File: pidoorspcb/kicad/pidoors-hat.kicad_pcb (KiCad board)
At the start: 2 copper layers, 65 x 56.5 mm, 4 parts

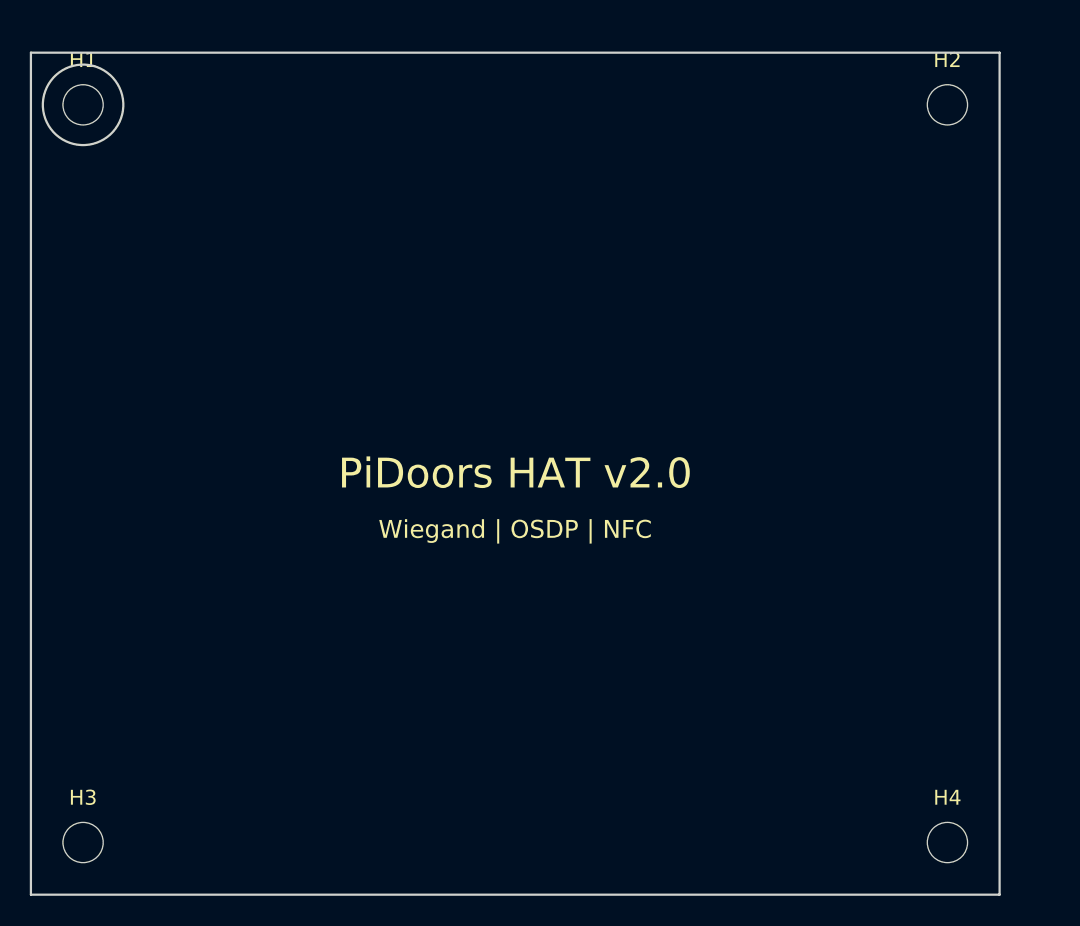
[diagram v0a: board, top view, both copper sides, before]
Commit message: PCB: Complete routing and generate Gerber manufacturing files
- Fix GPIO discrepancy: LED Granted now uses GPIO 25 (was GPIO 5)
- Fix README: Relay uses GPIO 18 (was incorrectly listed as GPIO 17)
- Complete KiCad schematic with all component symbols and connections
- Route PCB with power traces (0.5mm) and signal traces (0.25mm)
- Add ground plane on bottom copper layer
- Generate Gerber files in RS-274X format for JLCPCB
- Generate Excellon drill files (PTH and NPTH)
- Add manufacturing checklist with ordering instructions
- Add gerber generation script for KiCad 8.x

Co-Authored-By: Claude Opus 4.5 <noreply@anthropic.com>
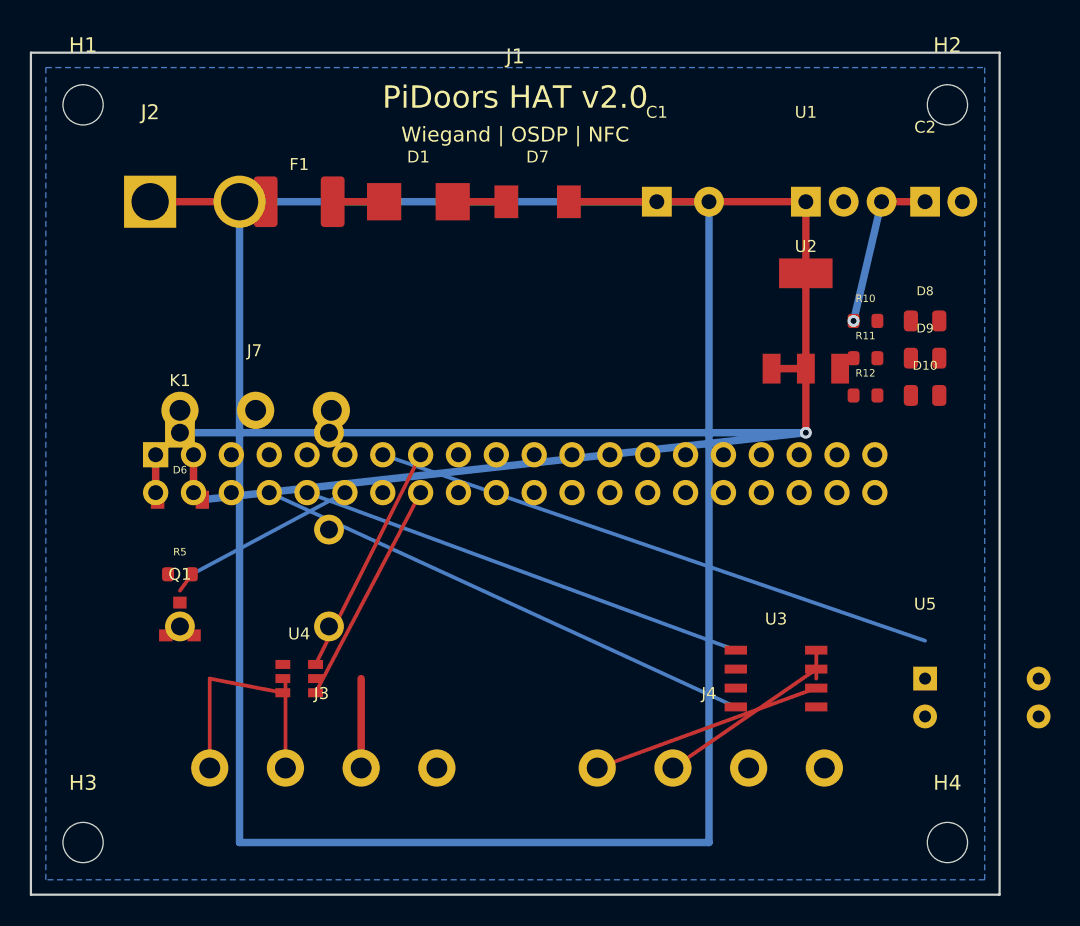
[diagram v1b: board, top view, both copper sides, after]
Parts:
- added C1: 100uF/35V, Capacitor_THT:CP_Radial_D8.0mm_P3.50mm, F.Cu at (42.0, 10.0)
- added C2: 100uF/10V, Capacitor_THT:CP_Radial_D6.3mm_P2.50mm, F.Cu at (60.0, 10.0)
- added D1: SMBJ24A, Diode_SMD:D_SMB, F.Cu at (26.0, 10.0)
- added D10: ERR, LED_SMD:LED_0805_2012Metric, F.Cu at (60.0, 23.0)
- added D6: 1N4148W, Diode_SMD:D_SOD-123, F.Cu at (10.0, 30.0)
- added D7: SS34, Diode_SMD:D_SMA, F.Cu at (34.0, 10.0)
- added D8: PWR, LED_SMD:LED_0805_2012Metric, F.Cu at (60.0, 18.0)
- added D9: OK, LED_SMD:LED_0805_2012Metric, F.Cu at (60.0, 20.5)
- added F1: 1.1A, Fuse:Fuse_1812_4532Metric, F.Cu at (18.0, 10.0)
- added J1: Raspberry_Pi, Connector_PinSocket_2.54mm:PinSocket_2x20_P2.54mm_Vertical, F.Cu at (32.5, 28.2)
- added J2: 12V DC, Connector_BarrelJack:BarrelJack_CUI_PJ-002A_Horizontal, F.Cu at (8.00, 10.0)
- added J3: Wiegand, TerminalBlock_Phoenix:TerminalBlock_Phoenix_MKDS-1,5-4-5.08_1x04_P5.08mm_Horizontal, F.Cu at (12.0, 48.0)
- added J4: RS485, TerminalBlock_Phoenix:TerminalBlock_Phoenix_MKDS-1,5-4-5.08_1x04_P5.08mm_Horizontal, F.Cu at (38.0, 48.0)
- added J7: Relay_Out, TerminalBlock_Phoenix:TerminalBlock_Phoenix_MKDS-1,5-3-5.08_1x03_P5.08mm_Horizontal, F.Cu at (10.0, 24.0)
- added K1: G5LE-14_DC12, Relay_THT:Relay_SPDT_Omron-G5LE-14, F.Cu at (10.0, 32.0)
- added Q1: MMBT2222A, Package_TO_SOT_SMD:SOT-23, F.Cu at (10.0, 38.0)
- added R10: 1k, Resistor_SMD:R_0603_1608Metric, F.Cu at (56.0, 18.0)
- added R11: 330, Resistor_SMD:R_0603_1608Metric, F.Cu at (56.0, 20.5)
- added R12: 220, Resistor_SMD:R_0603_1608Metric, F.Cu at (56.0, 23.0)
- added R5: 1k, Resistor_SMD:R_0603_1608Metric, F.Cu at (10.0, 35.0)
- added U1: OKI-78SR-5, Converter_DCDC:Converter_DCDC_muRata_OKI-78SRx_Vertical, F.Cu at (52.0, 10.0)
- added U2: LD1117S33, Package_TO_SOT_SMD:SOT-223-3_TabPin2, F.Cu at (52.0, 18.0)
- added U3: MAX13487E, Package_SO:SOIC-8_3.9x4.9mm_P1.27mm, F.Cu at (50.0, 42.0)
- added U4: TXB0102, Package_TO_SOT_SMD:SOT-23-6, F.Cu at (18.0, 42.0)
- added U5: PC817, Package_DIP:DIP-4_W7.62mm, F.Cu at (60.0, 42.0)
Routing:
- net GND: track 0.00 -> 149.0 mm
- net +12V_FUSED: track 0.00 -> 121.2 mm, vias 0 -> 1
- net GPIO27_DOOR: track 0.00 -> 38.5 mm, vias 0 -> 1
- net GPIO14_TX: track 0.00 -> 34.4 mm, vias 0 -> 1
- net GPIO15_RX: track 0.00 -> 30.6 mm, vias 0 -> 1
- net +5V: track 0.00 -> 22.2 mm, vias 0 -> 1
- net GPIO23_D1: track 0.00 -> 15.7 mm
- net RS485_A: track 0.00 -> 15.6 mm
- net GPIO24_D0: track 0.00 -> 15.2 mm
- net RS485_B: track 0.00 -> 11.7 mm
- net GPIO18_RELAY: track 0.00 -> 11.6 mm, vias 0 -> 1
- net WIEG_D0: track 0.00 -> 11.0 mm
- net +12V: track 0.00 -> 7.75 mm
- net WIEG_D1: track 0.00 -> 6.18 mm
- net +3V3: track 0.00 -> 4.20 mm
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- added copper zone on B.Cu, net GND
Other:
- outline, holes or cut-outs redrawn
- net class Default added: clearance 0.2, trace_width 0.25, via_dia 0.8, via_drill 0.4
- net class Power added: clearance 0.3, trace_width 0.5, via_dia 0.8, via_drill 0.4
- rule pad_to_mask_clearance: 0 -> 0.05
- board text added: "github.com/pidoors"
- board text removed: "github.com/sybethiesant/pidoors"
